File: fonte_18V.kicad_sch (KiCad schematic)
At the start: 12 parts, among them J101 IN, J102 Conn_01x02

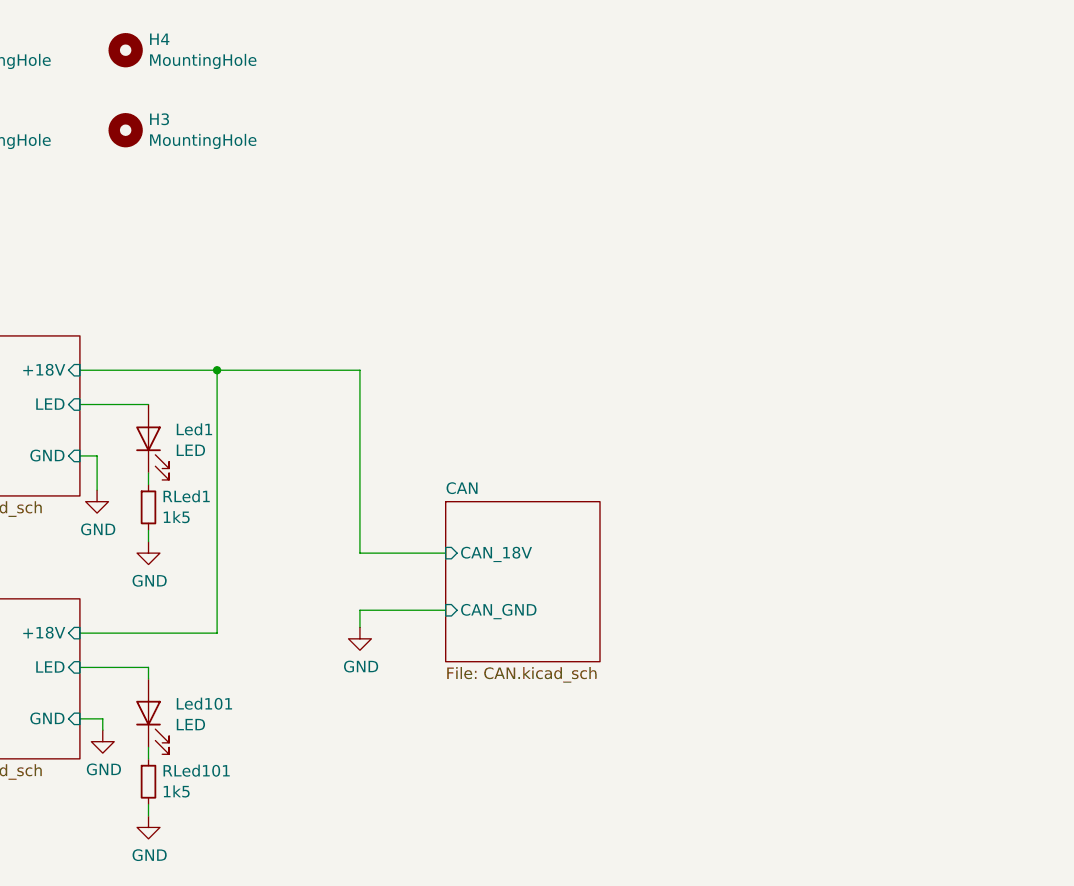
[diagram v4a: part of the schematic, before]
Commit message: Adjusted silkscreen and fixed RDC errors
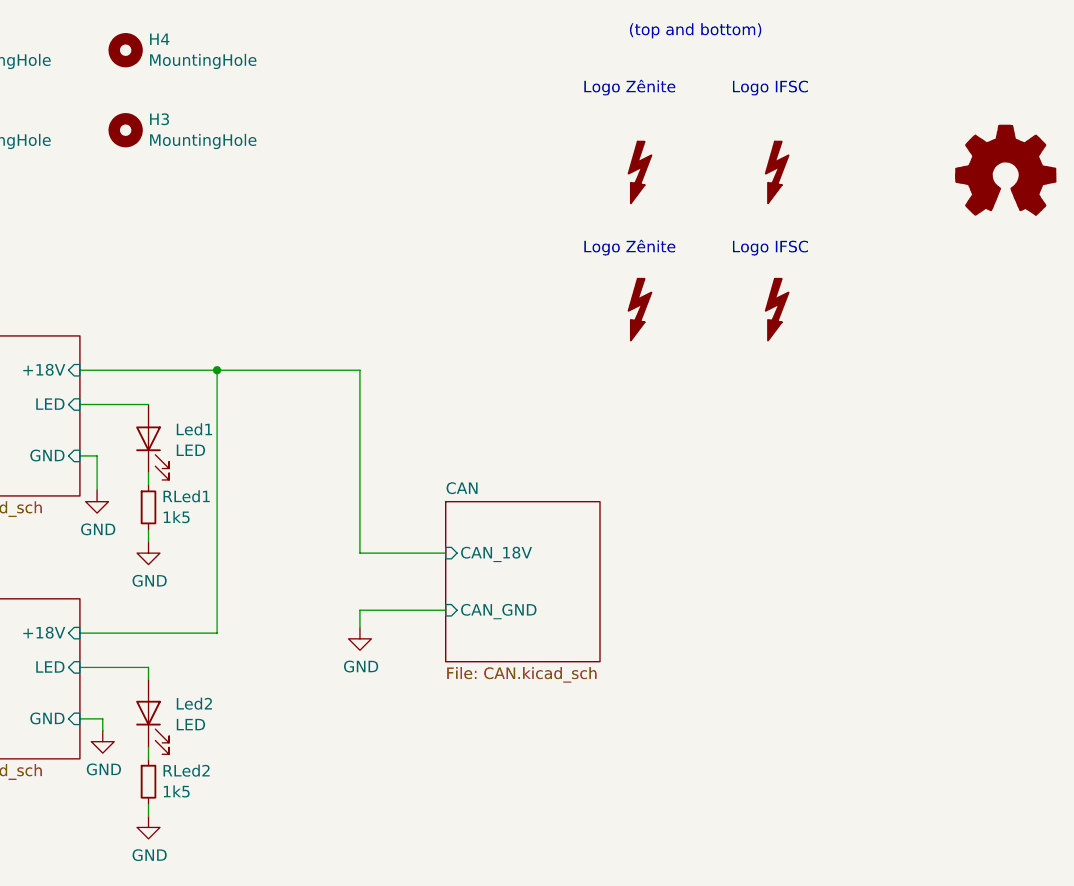
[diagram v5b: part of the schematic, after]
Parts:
- added LOGO101: (no value), symbol Graphic:Logo_Open_Hardware_Small
- added SYM101, SYM102: SYM_Flash_Small, KicadZeniteSolarLibrary18:symbol_logoZenite, symbol Graphic:SYM_Flash_Small
- added SYM103, SYM104: SYM_Flash_Small, KicadZeniteSolarLibrary18:synbol_logoifsc, symbol Graphic:SYM_Flash_Small
- renumbered Led101 to Led2, RLed101 to RLed2
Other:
- note added: "(top and bottom)"
- note added: "Logo IFSC"
- note added: "Logo Zênite"
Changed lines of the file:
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@@
     (stroke (width 0) (type default) (color 0 0 0 0))
+  )
+  (text "Logo Zênite" (at 133.35 60.96 0)
+    (effects (font (size 1.27 1.27)) (justify left bottom))
+  )
+  (text "Logo IFSC" (at 149.86 60.96 0)
+    (effects (font (size 1.27 1.27)) (justify left bottom))
+  )
+  (text "Logo IFSC" (at 149.86 78.74 0)
+    (effects (font (size 1.27 1.27)) (justify left bottom))
+  )
+  (text "(top and bottom)" (at 138.43 54.61 0)
+    (effects (font (size 1.27 1.27)) (justify left bottom))
+  )
+  (text "Logo Zênite" (at 133.35 78.74 0)
+    (effects (font (size 1.27 1.27)) (justify left bottom))
   )
   (label "EN" (at 49.53 91.44 0)
@@
   (symbol (lib_id "fonte_18V-rescue:R_Small-Device") (at 85.09 137.16 0) (unit 1)
     (in_bom yes) (on_board yes)
-    (property "Reference" "RLed101" (id 0) (at 86.5886 135.9916 0)
+    (property "Reference" "RLed2" (id 0) (at 86.5886 135.9916 0)
       (effects (font (size 1.27 1.27)) (justify left))
     )
@@
     (pin "1")
   )
+  (symbol (lib_id "Graphic:SYM_Flash_Small") (at 139.7 85.09 0) (unit 1)
+    (in_bom yes) (on_board yes) (fields_autoplaced)
+    (property "Reference" "SYM102" (id 0) (at 137.414 85.09 90)
+      (effects (font (size 1.27 1.27)) hide)
+    )
+    (property "Value" "SYM_Flash_Small" (id 1) (at 141.986 85.09 90)
+      (effects (font (size 1.27 1.27)) hide)
+    )
+    (property "Footprint" "KicadZeniteSolarLibrary18:symbol_logoZenite" (id 2) (at 139.7 85.725 0)
+      (effects (font (size 1.27 1.27)) hide)
+    )
+    (property "Datasheet" "~" (id 3) (at 149.86 87.63 0)
+      (effects (font (size 1.27 1.27)) hide)
+    )
+  )
+  (symbol (lib_id "Graphic:SYM_Flash_Small") (at 154.94 85.09 0) (unit 1)
+    (in_bom yes) (on_board yes) (fields_autoplaced)
+    (property "Reference" "SYM104" (id 0) (at 152.654 85.09 90)
+      (effects (font (size 1.27 1.27)) hide)
+    )
+    (property "Value" "SYM_Flash_Small" (id 1) (at 157.226 85.09 90)
+      (effects (font (size 1.27 1.27)) hide)
+    )
+    (property "Footprint" "KicadZeniteSolarLibrary18:synbol_logoifsc" (id 2) (at 154.94 85.725 0)
+      (effects (font (size 1.27 1.27)) hide)
+    )
+    (property "Datasheet" "~" (id 3) (at 165.1 87.63 0)
+      (effects (font (size 1.27 1.27)) hide)
+    )
+  )
   (symbol (lib_id "fonte_18V-rescue:GND-power") (at 108.585 120.015 0) (unit 1)
     (in_bom yes) (on_board yes)
@@
     (pin "1")
   )
+  (symbol (lib_id "Graphic:Logo_Open_Hardware_Small") (at 180.34 69.85 0) (unit 1)
+    (in_bom yes) (on_board yes) (fields_autoplaced)
+    (property "Reference" "LOGO101" (id 0) (at 180.34 62.865 0)
+      (effects (font (size 1.27 1.27)) hide)
+    )
+    (property "Value" "" (id 1) (at 180.34 75.565 0)
+      (effects (font (size 1.27 1.27)) hide)
+    )
+    (property "Footprint" "" (id 2) (at 180.34 69.85 0)
+      (effects (font (size 1.27 1.27)) hide)
+    )
+    (property "Datasheet" "~" (id 3) (at 180.34 69.85 0)
+      (effects (font (size 1.27 1.27)) hide)
+    )
+  )
   (symbol (lib_id "fonte_18V-rescue:LED-Device") (at 85.09 129.54 90) (unit 1)
     (in_bom yes) (on_board yes)
-    (property "Reference" "Led101" (id 0) (at 88.0618 128.5494 90)
+    (property "Reference" "Led2" (id 0) (at 88.0618 128.5494 90)
       (effects (font (size 1.27 1.27)) (justify right))
     )
@@
     (pin "2")
   )
+  (symbol (lib_id "Graphic:SYM_Flash_Small") (at 154.94 69.85 0) (unit 1)
+    (in_bom yes) (on_board yes) (fields_autoplaced)
+    (property "Reference" "SYM103" (id 0) (at 152.654 69.85 90)
+      (effects (font (size 1.27 1.27)) hide)
+    )
+    (property "Value" "SYM_Flash_Small" (id 1) (at 157.226 69.85 90)
+      (effects (font (size 1.27 1.27)) hide)
+    )
+    (property "Footprint" "KicadZeniteSolarLibrary18:synbol_logoifsc" (id 2) (at 154.94 70.485 0)
+      (effects (font (size 1.27 1.27)) hide)
+    )
+    (property "Datasheet" "~" (id 3) (at 165.1 72.39 0)
+      (effects (font (size 1.27 1.27)) hide)
+    )
+  )
   (symbol (lib_id "fonte_18V-rescue:GND-power") (at 85.09 140.97 0) (unit 1)
     (in_bom yes) (on_board yes)
@@
     )
     (pin "1")
+  )
+  (symbol (lib_id "Graphic:SYM_Flash_Small") (at 139.7 69.85 0) (unit 1)
+    (in_bom yes) (on_board yes) (fields_autoplaced)
+    (property "Reference" "SYM101" (id 0) (at 137.414 69.85 90)
+      (effects (font (size 1.27 1.27)) hide)
+    )
+    (property "Value" "SYM_Flash_Small" (id 1) (at 141.986 69.85 90)
+      (effects (font (size 1.27 1.27)) hide)
+    )
+    (property "Footprint" "KicadZeniteSolarLibrary18:symbol_logoZenite" (id 2) (at 139.7 70.485 0)
+      (effects (font (size 1.27 1.27)) hide)
+    )
+    (property "Datasheet" "~" (id 3) (at 149.86 72.39 0)
+      (effects (font (size 1.27 1.27)) hide)
+    )
   )
   (symbol (lib_id "Connector_Generic:Conn_01x03") (at 21.59 95.25 180) (unit 1)
@@
       (reference "L301") (unit 1) (value "100uH") (footprint "Inductor_THT:L_Radial_D21.0mm_P19.00mm")
     )
+    (path "/9f7324c5-50a2-442c-8a80-edf04aa2b2ac"
+      (reference "LOGO101") (unit 1) (value "Logo_Open_Hardware_Small") (footprint "Symbol:OSHW-Logo2_7.3x6mm_SilkScreen")
+    )
     (path "/00000000-0000-0000-0000-00005cbad6e9"
       (reference "Led1") (unit 1) (value "LED") (footprint "LED_SMD:LED_0805_2012Metric_Pad1.15x1.40mm_HandSolder")
     )
     (path "/adc8cb64-2a67-4af6-b1e3-82cd8137b605"
-      (reference "Led101") (unit 1) (value "LED") (footprint "LED_SMD:LED_0805_2012Metric_Pad1.15x1.40mm_HandSolder")
+      (reference "Led2") (unit 1) (value "LED") (footprint "LED_SMD:LED_0805_2012Metric_Pad1.15x1.40mm_HandSolder")
     )
     (path "/f584877a-9f43-4db0-b0ea-63e7b7af9907/035c22e3-96dd-47f6-9855-540743a87979"
@@
     )
     (path "/09741c8e-bc40-4216-bf8c-ade8568455cc"
-      (reference "RLed101") (unit 1) (value "1k5") (footprint "Resistor_SMD:R_0805_2012Metric_Pad1.20x1.40mm_HandSolder")
+      (reference "RLed2") (unit 1) (value "1k5") (footprint "Resistor_SMD:R_0805_2012Metric_Pad1.20x1.40mm_HandSolder")
     )
     (path "/f584877a-9f43-4db0-b0ea-63e7b7af9907/f6201bb6-7635-45f1-af2a-fcf727d179d5"
@@
       (reference "Rs301") (unit 1) (value "2k2") (footprint "Resistor_SMD:R_0805_2012Metric_Pad1.20x1.40mm_HandSolder")
     )
+    (path "/d73a16be-f88e-42ac-9769-63465a125122"
+      (reference "SYM101") (unit 1) (value "SYM_Flash_Small") (footprint "KicadZeniteSolarLibrary18:symbol_logoZenite")
+    )
+    (path "/5d708b1d-f53e-4c26-a11a-dd207e069a6f"
+      (reference "SYM102") (unit 1) (value "SYM_Flash_Small") (footprint "KicadZeniteSolarLibrary18:symbol_logoZenite")
+    )
+    (path "/c4390a62-a6e5-4c03-87f8-9d8cc2748e1e"
+      (reference "SYM103") (unit 1) (value "SYM_Flash_Small") (footprint "KicadZeniteSolarLibrary18:synbol_logoifsc")
+    )
+    (path "/7030a6ef-1b8c-4269-b26c-3341c1e35d96"
+      (reference "SYM104") (unit 1) (value "SYM_Flash_Small") (footprint "KicadZeniteSolarLibrary18:synbol_logoifsc")
+    )
     (path "/f584877a-9f43-4db0-b0ea-63e7b7af9907/c508f2e8-cf28-4e25-9367-14a77b11397b"
